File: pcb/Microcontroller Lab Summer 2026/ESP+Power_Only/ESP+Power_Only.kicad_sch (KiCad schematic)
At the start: 36 parts, among them J2 Power OUT, J3 SR_QH_Return, J4 Signals OUT, SW1 SW_Push, SW2 SW_Push, SW3 SW_Push, SW4 SW_Push, SW5 SW_SPDT, U1 TLV62568DBVR, U2 SN74AHCT125N, U4 TLV61048DBVR

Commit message: fixed PCB footprints, pending final review before order
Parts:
- C1, C4: footprint Capacitor_SMD:C_01005_0402Metric -> Capacitor_SMD:C_0402_1005Metric
- C2, C3, C5, C6, C7: footprint Capacitor_SMD:C_0201_0603Metric -> Capacitor_SMD:C_0603_1608Metric
- R11, R6: footprint Resistor_SMD:R_01005_0402Metric -> Resistor_SMD:R_0402_1005Metric
- R14, R9: footprint Resistor_SMD:R_0201_0603Metric -> Resistor_SMD:R_0603_1608Metric
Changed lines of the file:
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@@
 			)
 		)
-		(property "Footprint" "Capacitor_SMD:C_0201_0603Metric"
+		(property "Footprint" "Capacitor_SMD:C_0603_1608Metric"
 			(at 276.5552 45.72 0)
 			(hide yes)
@@
 			)
 		)
-		(property "Footprint" "Capacitor_SMD:C_0201_0603Metric"
+		(property "Footprint" "Capacitor_SMD:C_0603_1608Metric"
 			(at 43.4848 72.39 0)
 			(hide yes)
@@
 			)
 		)
-		(property "Footprint" "Resistor_SMD:R_0201_0603Metric"
+		(property "Footprint" "Resistor_SMD:R_0603_1608Metric"
 			(at 256.032 111.76 90)
 			(hide yes)
@@
 			)
 		)
-		(property "Footprint" "Resistor_SMD:R_01005_0402Metric"
+		(property "Footprint" "Resistor_SMD:R_0402_1005Metric"
 			(at 205.232 41.91 90)
 			(hide yes)
@@
 			)
 		)
-		(property "Footprint" "Capacitor_SMD:C_0201_0603Metric"
+		(property "Footprint" "Capacitor_SMD:C_0603_1608Metric"
 			(at 197.8152 45.72 0)
 			(hide yes)
@@
 			)
 		)
-		(property "Footprint" "Capacitor_SMD:C_01005_0402Metric"
+		(property "Footprint" "Capacitor_SMD:C_0402_1005Metric"
 			(at 35.56 33.3248 0)
 			(hide yes)
@@
 			)
 		)
-		(property "Footprint" "Capacitor_SMD:C_0201_0603Metric"
+		(property "Footprint" "Capacitor_SMD:C_0603_1608Metric"
 			(at 201.6252 111.76 0)
 			(hide yes)
@@
 			)
 		)
-		(property "Footprint" "Resistor_SMD:R_0201_0603Metric"
+		(property "Footprint" "Resistor_SMD:R_0603_1608Metric"
 			(at 205.232 62.23 90)
 			(hide yes)
@@
 			)
 		)
-		(property "Footprint" "Capacitor_SMD:C_01005_0402Metric"
+		(property "Footprint" "Capacitor_SMD:C_0402_1005Metric"
 			(at 32.0548 72.39 0)
 			(hide yes)
@@
 			)
 		)
-		(property "Footprint" "Capacitor_SMD:C_0201_0603Metric"
+		(property "Footprint" "Capacitor_SMD:C_0603_1608Metric"
 			(at 270.2052 110.49 0)
 			(hide yes)
@@
 			)
 		)
-		(property "Footprint" "Resistor_SMD:R_01005_0402Metric"
+		(property "Footprint" "Resistor_SMD:R_0402_1005Metric"
 			(at 256.032 101.6 90)
 			(hide yes)

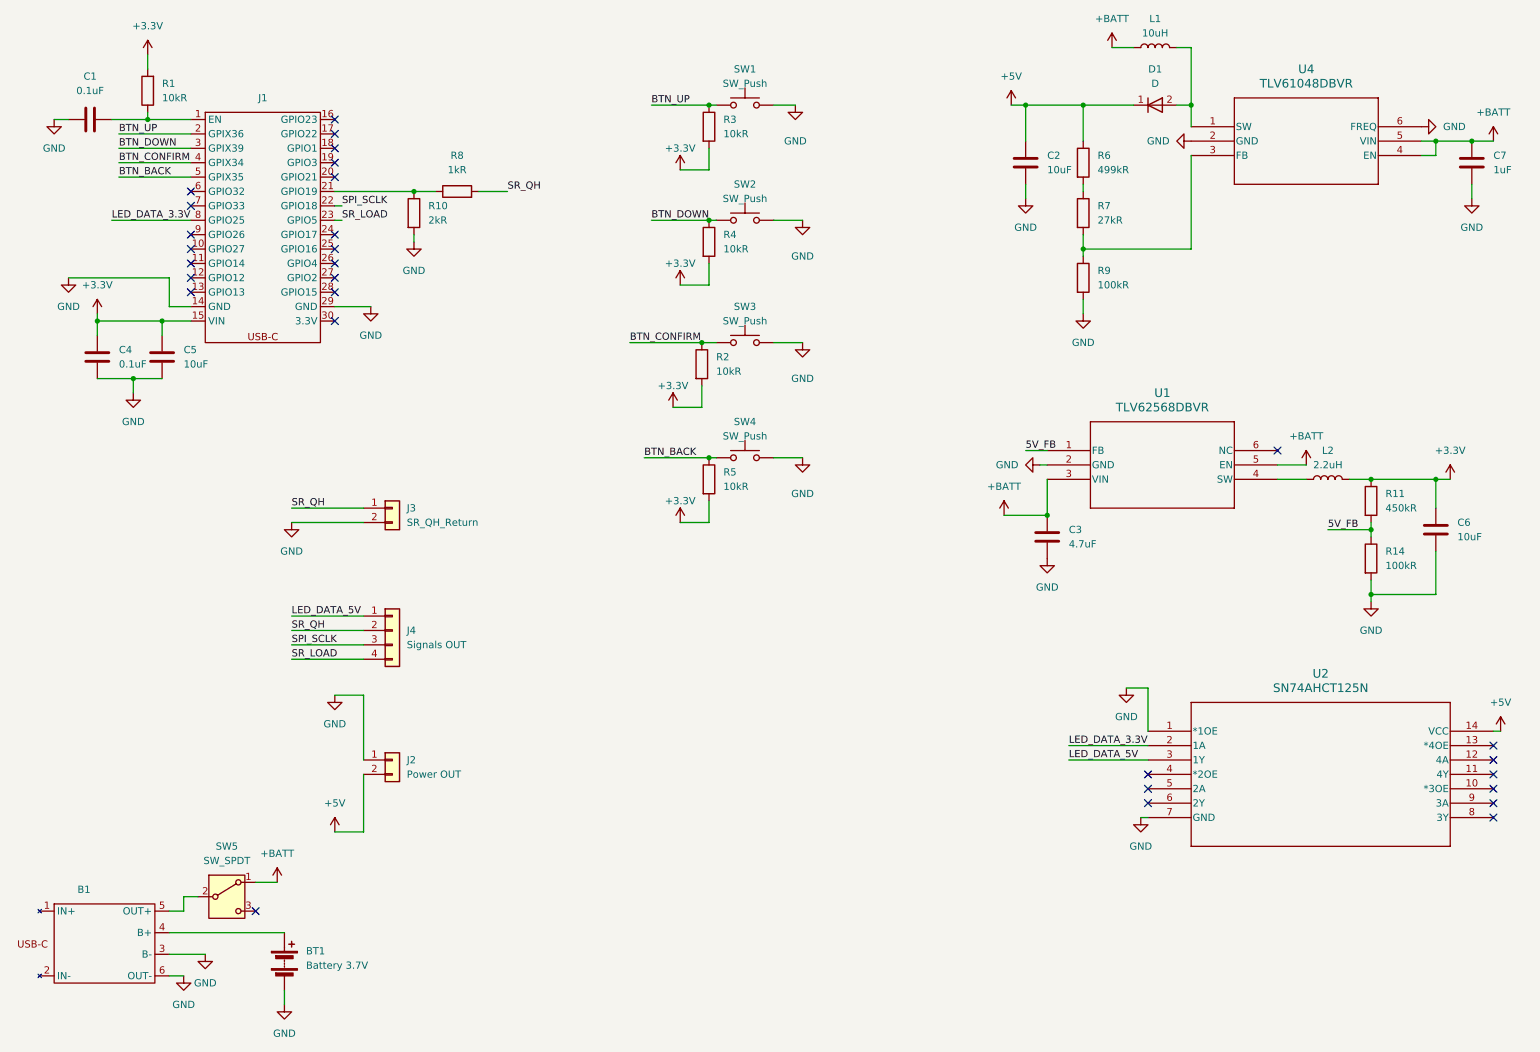
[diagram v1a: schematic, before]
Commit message: fixed detection pcb dip-16 footprint. fixed esp pcb charger board polarity, minor trace adjustments, level shifting for spi sclk and shift register mode signals. fixed charger board polarity footprint. last fix remaining is to get a more precise measurement for the two front pins on the charger board and update accordingly
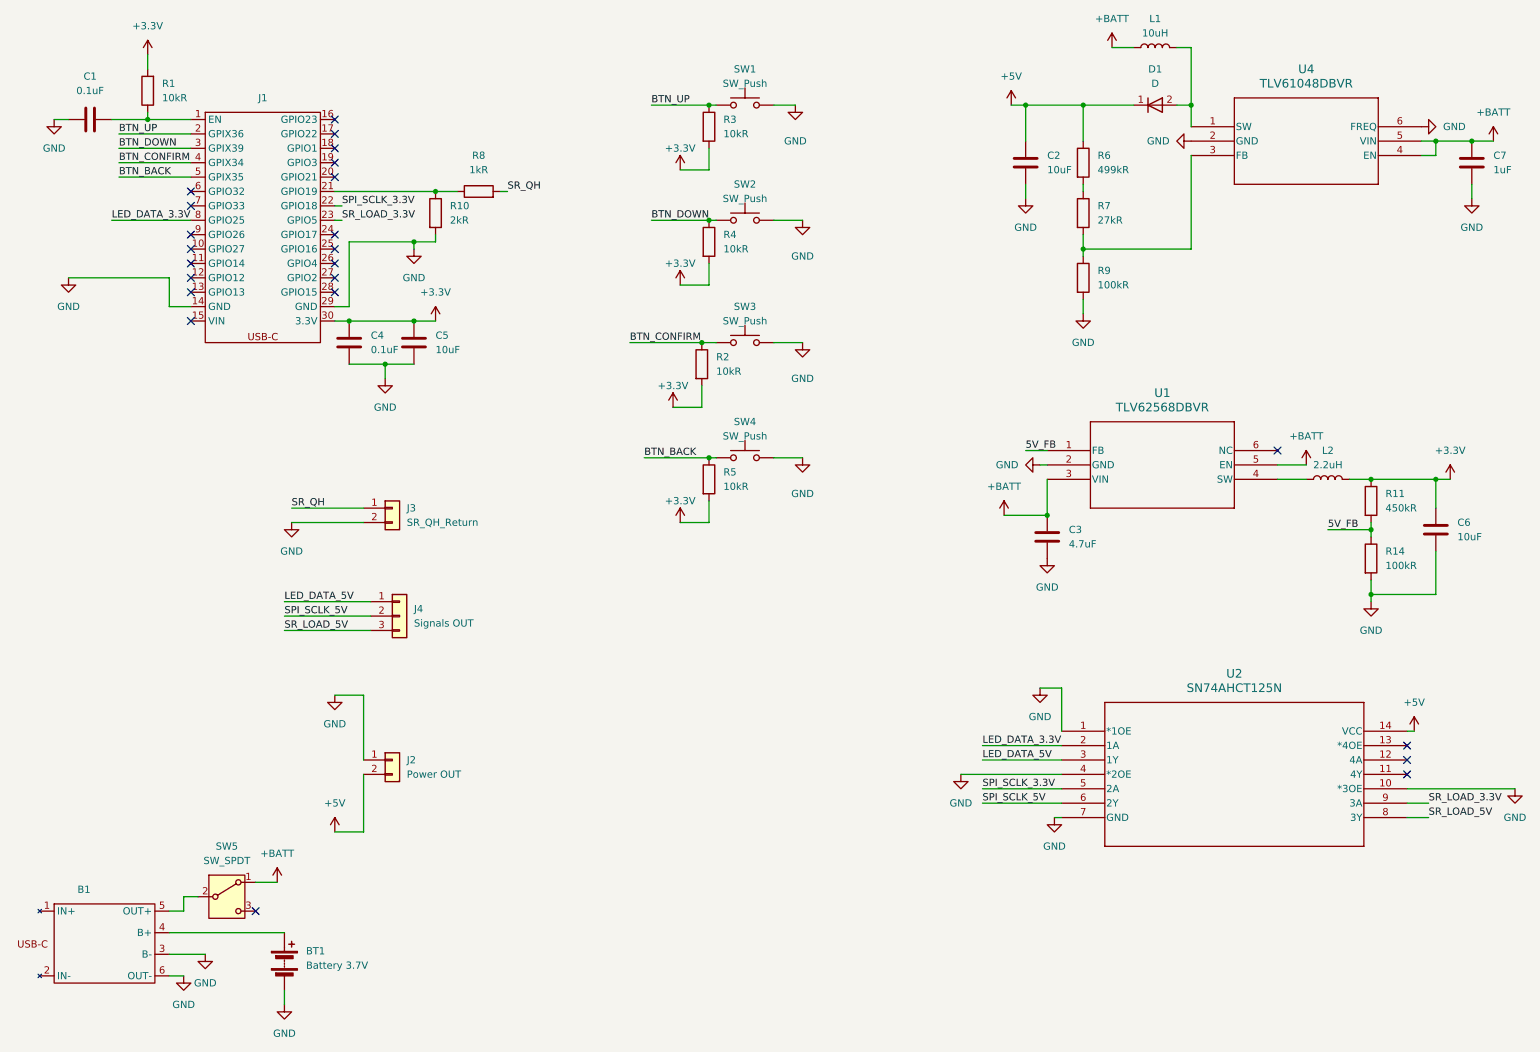
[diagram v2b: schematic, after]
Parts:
- removed J4: Signals OUT, Connector_PinHeader_2.54mm:PinHeader_1x04_P2.54mm_Vertical, symbol Connector_Generic:Conn_01x04
- added J4: Signals OUT, Connector_PinHeader_2.54mm:PinHeader_1x03_P2.54mm_Vertical, symbol Connector_Generic:Conn_01x03
- BT1: footprint ChessLink:battery_outline -> (none)
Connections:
- net SPI_SCLK is gone; now on net SPI_SCLK_3.3V: J1.22 (GPIO18)
- net SR_LOAD is gone; now on net SR_LOAD_3.3V: J1.23 (GPIO5)
- net +3.3V: now also J1.30 (3.3V); no longer J1.15 (VIN)
- net GND: now also U2.10 (*3OE), U2.4 (*2OE)
- net LED_DATA_5V: now also J4.1 (Pin_1)
- net SPI_SCLK_3.3V: now reaches U2.5 (2A)
- net SPI_SCLK_5V: now reaches U2.6 (2Y)
- net SPI_SCLK_5V: now also J4.2 (Pin_2)
- net SR_LOAD_5V: now reaches U2.8 (3Y)
- net SR_LOAD_5V: now also J4.3 (Pin_3)
- net SR_LOAD_3.3V: now reaches U2.9 (3A)
- no-connect marks 29 -> 23
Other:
- moved on the sheet: C4, C5, R10, R8, U2
